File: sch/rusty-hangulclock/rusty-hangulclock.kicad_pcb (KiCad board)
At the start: 2 copper layers, 53.5 x 54 mm, 13 parts, among them J1 Conn_OLED, J2 Conn_LEDS, J3 PWR, SW1 SW_Push

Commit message: fix sch and pcb
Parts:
- added G***: LOGO, LOGO, F.Cu at (168.2, 114.0)
- added REF**: OSHW-Logo2_7.3x6mm_SilkScreen, Symbol:OSHW-Logo2_7.3x6mm_SilkScreen, F.Cu at (158.1, 104.3)
- added SW2: SW_Push, Button_Switch_THT:SW_PUSH_6mm, F.Cu at (140.7, 98.7)
- J1: footprint Connector_PinHeader_2.54mm:PinHeader_1x05_P2.54mm_Horizontal -> Connector_PinHeader_2.54mm:PinHeader_1x04_P2.54mm_Vertical
- moved H1 72.9 mm to (171.3, 79.8), turned to 180 degrees
- moved H2 66.2 mm to (171.3, 125.8), turned to 180 degrees
- moved H4 65.4 mm to (125.3, 79.8), turned to 180 degrees
- moved H3 57.9 mm to (125.3, 125.8), turned to 180 degrees
- moved J1 51.5 mm to (152.0, 78.4), turned to -90 degrees
- moved J2 41.8 mm to (164.3, 88.8), turned to 0 degrees
- moved RV1 35.4 mm to (154.4, 90.5), turned to 180 degrees
- moved D1 30.6 mm to (159.1, 84.2), turned to -90 degrees
- moved SW1 30.5 mm to (140.8, 90.5), turned to 180 degrees
- moved R1 29.2 mm to (159.1, 96.9)
- moved ESP32-C3_SuperMini1 27.4 mm to (141.3, 118.2), turned to 180 degrees
- moved J3 5.65 mm to (160.1, 119.0)
- moved C1 5.45 mm to (159.5, 113.0)
- renumbered M1 to ESP32-C3_SuperMini1, H4 to H1, H3 to H2, H2 to H3, H1 to H4
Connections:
- ESP32-C3_SuperMini1 pad 10: Net-(J1-Pin_5) -> Net-(ESP32-C3_SuperMini1-P10)
- ESP32-C3_SuperMini1 pad 8: Net-(J1-Pin_3) -> Net-(ESP32-C3_SuperMini1-P8)
- ESP32-C3_SuperMini1 pad 9: Net-(J1-Pin_4) -> Net-(ESP32-C3_SuperMini1-P9)
- J1 pad 3: Net-(J1-Pin_3) -> Net-(ESP32-C3_SuperMini1-P9)
- J1 pad 4: Net-(J1-Pin_4) -> Net-(ESP32-C3_SuperMini1-P8)
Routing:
- net Net-(ESP32-C3_SuperMini1-P8): track 0.00 -> 48.3 mm, vias 0 -> 1
- net Net-(ESP32-C3_SuperMini1-P9): track 0.00 -> 44.3 mm
- net Net-(J1-Pin_3): track 40.9 -> 0.00 mm
- net Net-(J1-Pin_4): track 36.2 -> 0.00 mm
- net +5V: track 102.6 -> 66.9 mm
- net Net-(ESP32-C3_SuperMini1-P10): track 0.00 -> 32.3 mm
- net Net-(J1-Pin_5): track 31.6 -> 0.00 mm
- net Net-(ESP32-C3_SuperMini1-P6): track 26.0 -> 46.9 mm, vias 1 -> 2
- net Net-(ESP32-C3_SuperMini1-P7): track 15.4 -> 35.2 mm
- net Net-(ESP32-C3_SuperMini1-P2): track 21.3 -> 37.8 mm
- net Net-(ESP32-C3_SuperMini1-P5): track 26.5 -> 41.4 mm
- net Net-(ESP32-C3_SuperMini1-P1): track 27.3 -> 36.6 mm
- net Net-(ESP32-C3_SuperMini1-P3): track 33.7 -> 42.2 mm
- net GND: track 126.1 -> 131.5 mm
- net Net-(ESP32-C3_SuperMini1-P4): track 42.0 -> 46.3 mm, vias 2 -> 1
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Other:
- board size 53.5 x 54 mm -> 53 x 53.5 mm
- board text added: "Rusty HangulClock By Homin Lee Jan 2025 https://github.com/suapapa/HangulClock"
- board text removed: "P10"
- board text removed: "Rusty HangulClock By Homin Lee Jan 2025"

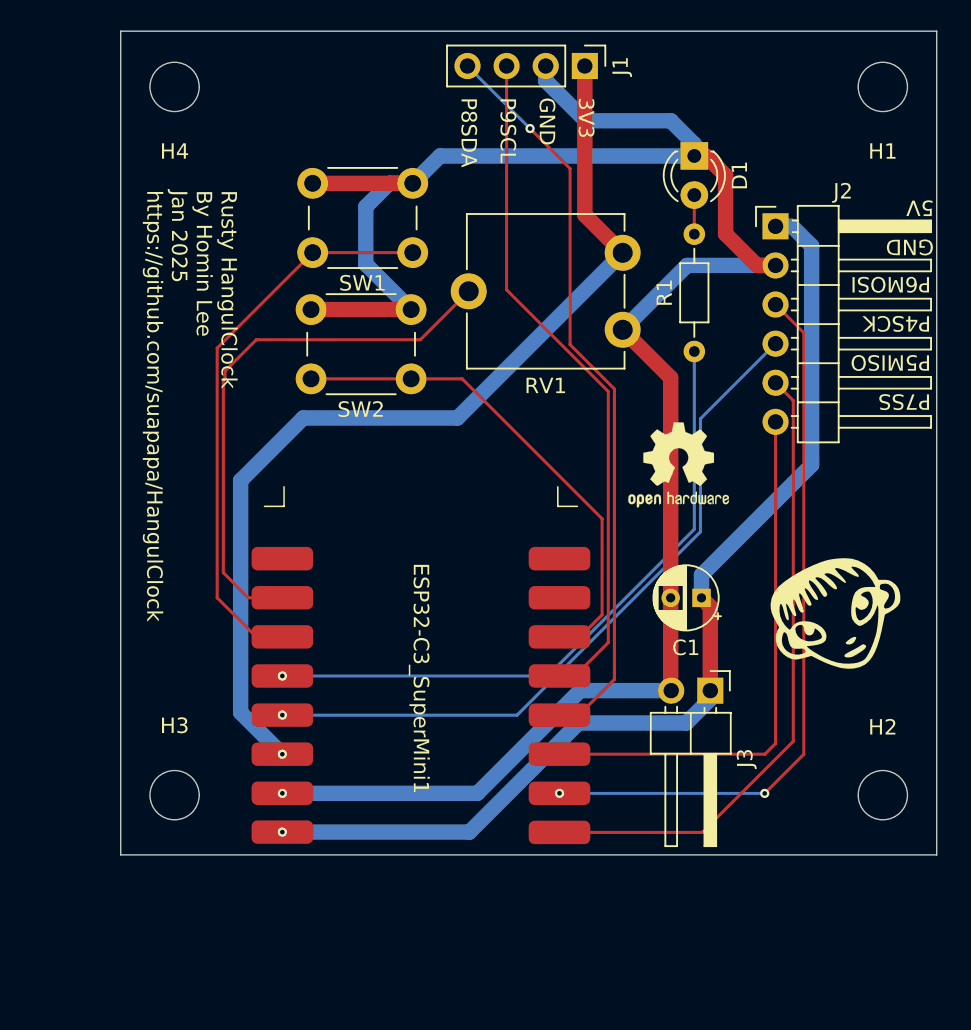
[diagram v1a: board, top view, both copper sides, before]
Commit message: split code to files
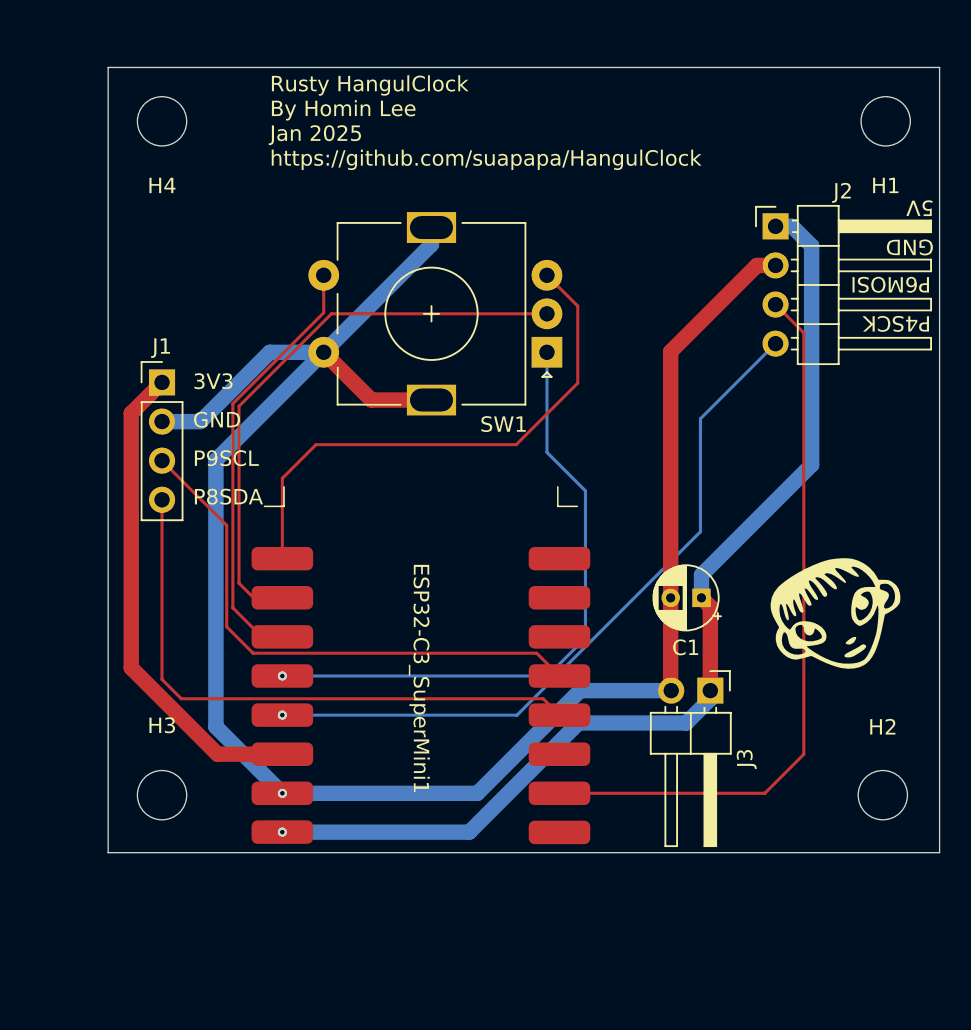
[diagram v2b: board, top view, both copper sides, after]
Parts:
- removed D1: LED, LED_THT:LED_D3.0mm
- removed R1: R, Resistor_THT:R_Axial_DIN0204_L3.6mm_D1.6mm_P7.62mm_Horizontal
- removed REF**: OSHW-Logo2_7.3x6mm_SilkScreen, Symbol:OSHW-Logo2_7.3x6mm_SilkScreen
- removed RV1: R_Potentiometer, Potentiometer_THT:Potentiometer_ACP_CA9-V10_Vertical
- removed SW2: SW_Push, Button_Switch_THT:SW_PUSH_6mm
- J2: value Conn_LEDS -> Conn_SLEDS; footprint Connector_PinHeader_2.54mm:PinHeader_1x06_P2.54mm_Horizontal -> Connector_PinHeader_2.54mm:PinHeader_1x04_P2.54mm_Horizontal
- SW1: value SW_Push -> RotaryEncoder_Switch_MP; footprint Button_Switch_THT:SW_PUSH_6mm -> Rotary_Encoder:RotaryEncoder_Alps_EC11E-Switch_Vertical_H20mm
- moved J1 34.3 mm to (124.5, 99.0), turned to 0 degrees
- moved SW1 10.9 mm to (149.5, 97.0)
- moved H4 2.38 mm to (124.5, 82.0)
- moved H1 2.24 mm to (171.5, 82.0)
- moved H3 0.81 mm to (124.5, 125.8)
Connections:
- ESP32-C3_SuperMini1 pad 0: unconnected-(ESP32-C3_SuperMini1-P0-Pad0) -> Net-(ESP32-C3_SuperMini1-P0)
- ESP32-C3_SuperMini1 pad 10: Net-(ESP32-C3_SuperMini1-P10) -> unconnected-(ESP32-C3_SuperMini1-P10-Pad10)
- ESP32-C3_SuperMini1 pad 5: Net-(ESP32-C3_SuperMini1-P5) -> unconnected-(ESP32-C3_SuperMini1-P5-Pad5)
- ESP32-C3_SuperMini1 pad 7: Net-(ESP32-C3_SuperMini1-P7) -> unconnected-(ESP32-C3_SuperMini1-P7-Pad7)
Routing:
- net Net-(ESP32-C3_SuperMini1-P5): track 41.4 -> 0.00 mm
- net Net-(ESP32-C3_SuperMini1-P7): track 35.2 -> 0.00 mm
- net Net-(ESP32-C3_SuperMini1-P0): track 0.00 -> 34.8 mm
- net Net-(ESP32-C3_SuperMini1-P10): track 32.3 -> 0.00 mm
- net +3V3: track 63.0 -> 31.5 mm, vias 1 -> 0
- net Net-(ESP32-C3_SuperMini1-P8): track 48.3 -> 38.4 mm, vias 1 -> 0
- net Net-(ESP32-C3_SuperMini1-P2): track 37.8 -> 28.0 mm
- net Net-(ESP32-C3_SuperMini1-P9): track 44.3 -> 35.5 mm
- net GND: track 131.5 -> 124.2 mm
- net Net-(D1-A): track 2.54 -> 0.00 mm
- net Net-(ESP32-C3_SuperMini1-P3): track 42.2 -> 40.3 mm
- net Net-(ESP32-C3_SuperMini1-P1): track 36.6 -> 37.2 mm
- net Net-(ESP32-C3_SuperMini1-P6): vias 2 -> 0
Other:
- board size 53 x 53.5 mm -> 54 x 51 mm
- board text removed: "P5MISO"
- board text removed: "P7SS"

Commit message: sch: re-draw sch and artwork for v1.0.0
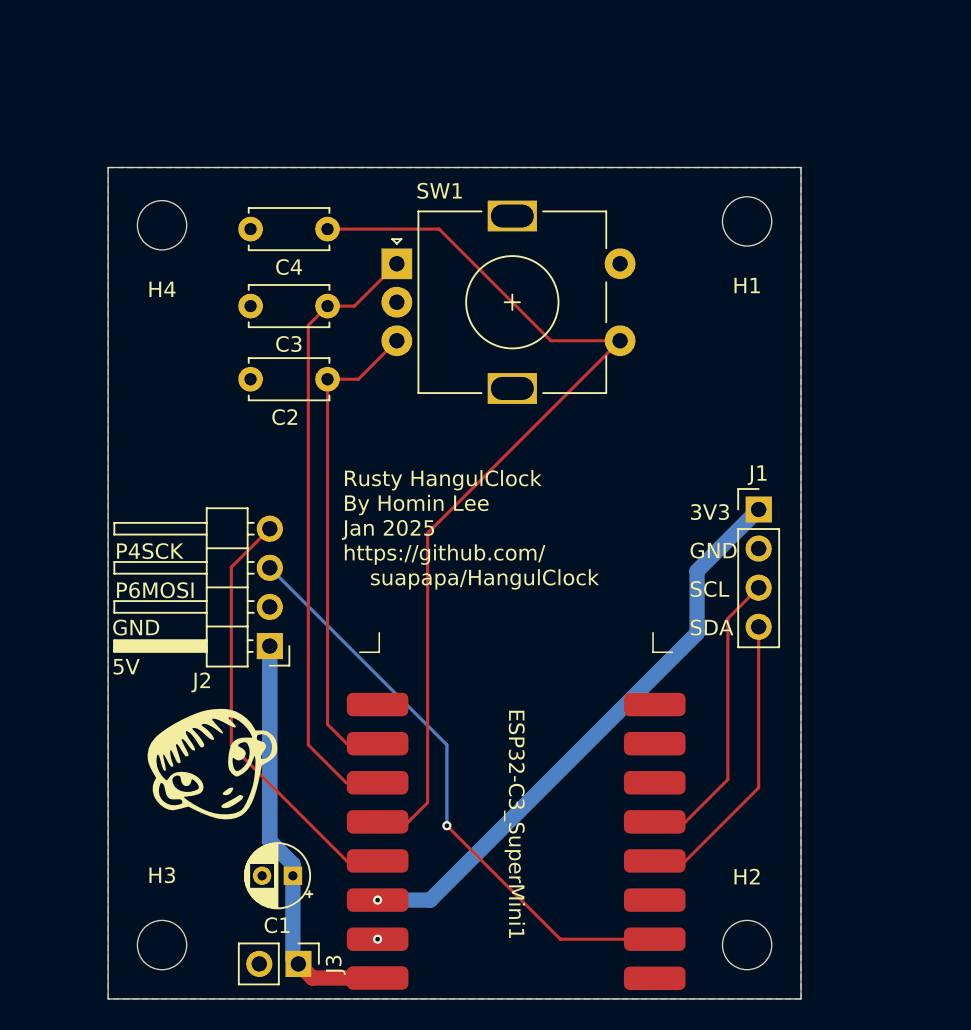
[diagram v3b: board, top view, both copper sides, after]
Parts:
- added C2: 100n, Capacitor_THT:C_Disc_D5.0mm_W2.5mm_P5.00mm, F.Cu at (135.2, 98.8)
- added C3: 100n, Capacitor_THT:C_Disc_D5.0mm_W2.5mm_P5.00mm, F.Cu at (135.2, 94.0)
- added C4: 100n, Capacitor_THT:C_Disc_D5.0mm_W2.5mm_P5.00mm, F.Cu at (135.2, 89.0)
- J3: footprint Connector_PinHeader_2.54mm:PinHeader_1x02_P2.54mm_Horizontal -> Connector_PinHeader_2.54mm:PinHeader_1x02_P2.54mm_Vertical
- moved J2 42.7 mm to (131.5, 116.1), turned to 180 degrees
- moved G*** 41.6 mm to (127.8, 123.8)
- moved J1 39.6 mm to (163.2, 107.2)
- moved J3 32.1 mm to (133.4, 136.7)
- moved C1 32.1 mm to (133.0, 131.0)
- moved H2 13.1 mm to (162.5, 135.5)
- moved SW1 11.3 mm to (139.8, 91.2), turned to 0 degrees
- moved ESP32-C3_SuperMini1 11.3 mm to (147.5, 127.7)
- moved H1 11.1 mm to (162.5, 88.5)
- moved H3 9.74 mm to (124.5, 135.5)
- moved H4 6.75 mm to (124.5, 88.8)
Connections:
- ESP32-C3_SuperMini1 pad 0: Net-(ESP32-C3_SuperMini1-P0) -> unconnected-(ESP32-C3_SuperMini1-P0-Pad0)
- SW1 pad A: Net-(ESP32-C3_SuperMini1-P3) -> Net-(ESP32-C3_SuperMini1-P2)
- SW1 pad B: Net-(ESP32-C3_SuperMini1-P0) -> Net-(ESP32-C3_SuperMini1-P1)
- SW1 pad C: Net-(ESP32-C3_SuperMini1-P1) -> GND
- SW1 pad S1: Net-(ESP32-C3_SuperMini1-P2) -> Net-(ESP32-C3_SuperMini1-P3)
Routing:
- net GND: track 124.2 -> 0.00 mm
- net +5V: track 66.9 -> 26.9 mm, vias 1 -> 0
- net Net-(ESP32-C3_SuperMini1-P0): track 34.8 -> 0.00 mm
- net Net-(ESP32-C3_SuperMini1-P3): track 40.3 -> 60.9 mm, vias 1 -> 0
- net Net-(ESP32-C3_SuperMini1-P8): track 38.4 -> 19.2 mm
- net Net-(ESP32-C3_SuperMini1-P4): track 46.3 -> 27.7 mm, vias 1 -> 0
- net Net-(ESP32-C3_SuperMini1-P9): track 35.5 -> 19.2 mm
- net Net-(ESP32-C3_SuperMini1-P2): track 28.0 -> 40.6 mm
- net Net-(ESP32-C3_SuperMini1-P6): track 46.9 -> 38.1 mm, vias 0 -> 1
- net +3V3: track 31.5 -> 37.6 mm, vias 0 -> 1
- net Net-(ESP32-C3_SuperMini1-P1): track 37.2 -> 31.7 mm
- added copper zone on B.Cu, net GND
- added copper zone on F.Cu, net GND
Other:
- board size 54 x 51 mm -> 45 x 54 mm
- board text added: "Rusty HangulClock By Homin Lee Jan 2025 https://github.com/ suapapa/HangulClock"
- board text added: "SCL"
- board text added: "SDA"
- board text removed: "P8SDA"
- board text removed: "P9SCL"
- board text removed: "Rusty HangulClock By Homin Lee Jan 2025 https://github.com/suapapa/HangulClock"

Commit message: sch: fix pcb
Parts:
- moved H4 0.25 mm to (124.5, 88.5)
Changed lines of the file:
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@@
 		)
 		(fp_text user "${REFERENCE}"
-			(at 0 1.27 360)
+			(at 0 1.27 0)
 			(layer "F.Fab")
 			(effects
@@
 		(tags "C Disc series Radial pin pitch 5.00mm  diameter 5mm width 2.5mm Capacitor")
 		(property "Reference" "C4"
-			(at 2.5 -2.5 360)
+			(at 2.5 -2.5 0)
 			(layer "F.SilkS")
 			(effects
@@
 		)
 		(property "Value" "100n"
-			(at 2.5 2.5 360)
+			(at 2.5 2.5 0)
 			(layer "F.Fab")
 			(effects
@@
 		)
 		(fp_text user "${REFERENCE}"
-			(at 2.5 0 360)
+			(at 2.5 0 0)
 			(layer "F.Fab")
 			(effects
@@
 		(tags "rotary encoder")
 		(property "Reference" "SW1"
-			(at 2.8 -4.7 360)
+			(at 2.8 -4.7 0)
 			(layer "F.SilkS")
 			(effects
@@
 		)
 		(property "Value" "RotaryEncoder_Switch_MP"
-			(at 7.5 10.4 360)
+			(at 7.5 10.4 0)
 			(layer "F.Fab")
 			(effects
@@
 		)
 		(fp_text user "${REFERENCE}"
-			(at 11.1 6.3 360)
+			(at 11.1 6.3 0)
 			(layer "F.Fab")
 			(effects
@@
 		(tags "C Disc series Radial pin pitch 5.00mm  diameter 5mm width 2.5mm Capacitor")
 		(property "Reference" "C2"
-			(at 2.75 -2.5 360)
+			(at 2.75 -2.5 0)
 			(layer "F.SilkS")
 			(effects
@@
 		)
 		(property "Value" "100n"
-			(at 2.5 2.5 360)
+			(at 2.5 2.5 0)
 			(layer "F.Fab")
 			(effects
@@
 		)
 		(fp_text user "${REFERENCE}"
-			(at 2.5 0 360)
+			(at 2.5 0 0)
 			(layer "F.Fab")
 			(effects
@@
 		(tags "Through hole angled pin header THT 1x04 2.54mm single row")
 		(property "Reference" "J2"
-			(at 4.385 -2.27 360)
+			(at 4.385 -2.27 0)
 			(layer "F.SilkS")
 			(effects
@@
 		)
 		(property "Value" "Conn_SLEDS"
-			(at 4.385 9.89 360)
+			(at 4.385 9.89 0)
 			(layer "F.Fab")
 			(effects
@@
 	(footprint "MountingHole:MountingHole_3.2mm_M3"
 		(layer "F.Cu")
-		(at 124.5 88.75 180)
+		(at 124.5 88.5 180)
 		(descr "Mounting Hole 3.2mm, no annular, M3")
 		(tags "mounting hole 3.2mm no annular m3")
@@
 		(tags "CP Radial series Radial pin pitch 2.00mm  diameter 4mm Electrolytic Capacitor")
 		(property "Reference" "C1"
-			(at 1 -3.25 360)
+			(at 1 -3.25 0)
 			(layer "F.SilkS")
 			(effects
@@
 		)
 		(property "Value" "C_Polarized"
-			(at 1 3.25 360)
+			(at 1 3.25 0)
 			(layer "F.Fab")
 			(effects
@@
 		)
 		(fp_text user "${REFERENCE}"
-			(at 1 0 360)
+			(at 1 0 0)
 			(layer "F.Fab")
 			(effects
@@
 		(at 127.75 123.75)
 		(property "Reference" "G***"
-			(at 0 0 360)
+			(at 0 0 0)
 			(layer "F.SilkS")
 			(hide yes)
@@
 		)
 		(property "Value" "LOGO"
-			(at 0.75 0 360)
+			(at 0.75 0 0)
 			(layer "F.SilkS")
 			(hide yes)
@@
 		)
 		(property "Footprint" ""
-			(at 0 0 360)
+			(at 0 0 0)
 			(layer "F.Fab")
 			(hide yes)
@@
 		)
 		(property "Datasheet" ""
-			(at 0 0 360)
+			(at 0 0 0)
 			(layer "F.Fab")
 			(hide yes)
@@
 		)
 		(property "Description" ""
-			(at 0 0 360)
+			(at 0 0 0)
 			(layer "F.Fab")
 			(hide yes)
@@
 		(tags "C Disc series Radial pin pitch 5.00mm  diameter 5mm width 2.5mm Capacitor")
 		(property "Reference" "C3"
-			(at 2.5 -2.5 360)
+			(at 2.5 -2.5 0)
 			(layer "F.SilkS")
 			(effects
@@
 		)
 		(property "Value" "100n"
-			(at 2.5 2.5 360)
+			(at 2.5 2.5 0)
 			(layer "F.Fab")
 			(effects
@@
 		)
 		(fp_text user "${REFERENCE}"
-			(at 2.5 0 360)
+			(at 2.5 0 0)
 			(layer "F.Fab")
 			(effects

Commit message: fix pcb
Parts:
- moved J1 8.79 mm to (163.2, 116.0), turned to 180 degrees
- moved J2 0.08 mm to (131.5, 116.0)
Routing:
- net Net-(ESP32-C3_SuperMini1-P8): track 19.2 -> 29.4 mm
- net +3V3: track 37.6 -> 31.6 mm
- net Net-(ESP32-C3_SuperMini1-P9): track 19.2 -> 20.9 mm
- net Net-(ESP32-C3_SuperMini1-P4): track 27.7 -> 28.6 mm
- net Net-(ESP32-C3_SuperMini1-P6): track 38.1 -> 38.7 mm

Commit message: update sch and gerber
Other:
- board text added: "Rusty HangulClock By Homin Lee Feb 2025 https://github.com/ suapapa/HangulClock"
- board text removed: "Rusty HangulClock By Homin Lee Jan 2025 https://github.com/ suapapa/HangulClock"
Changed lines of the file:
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@@
 		(tags "Through hole pin header THT 1x04 2.54mm single row")
 		(property "Reference" "J1"
-			(at 0 -2.33 360)
+			(at 0 -2.33 0)
 			(layer "F.SilkS")
 			(effects
@@
 		)
 		(property "Value" "Conn_OLED"
-			(at 0 9.95 360)
+			(at 0 9.95 0)
 			(layer "F.Fab")
 			(effects
@@
 		)
 	)
-	(gr_text "Rusty HangulClock\nBy Homin Lee\nJan 2025\nhttps://github.com/\n	suapapa/HangulClock"
+	(gr_text "Rusty HangulClock\nBy Homin Lee\nFeb 2025\nhttps://github.com/\n	suapapa/HangulClock"
 		(at 136.25 112.25 0)
 		(layer "F.SilkS")
